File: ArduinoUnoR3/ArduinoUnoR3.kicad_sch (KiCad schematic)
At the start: 40 parts, among them J1 USB_B_Micro, SW1 SW_Push, U1 ATmega16U2-A, U2 LMV358, U3 LMV358, U4 ATmega328PB-A, Y1 16MHz, Y2 16MHz

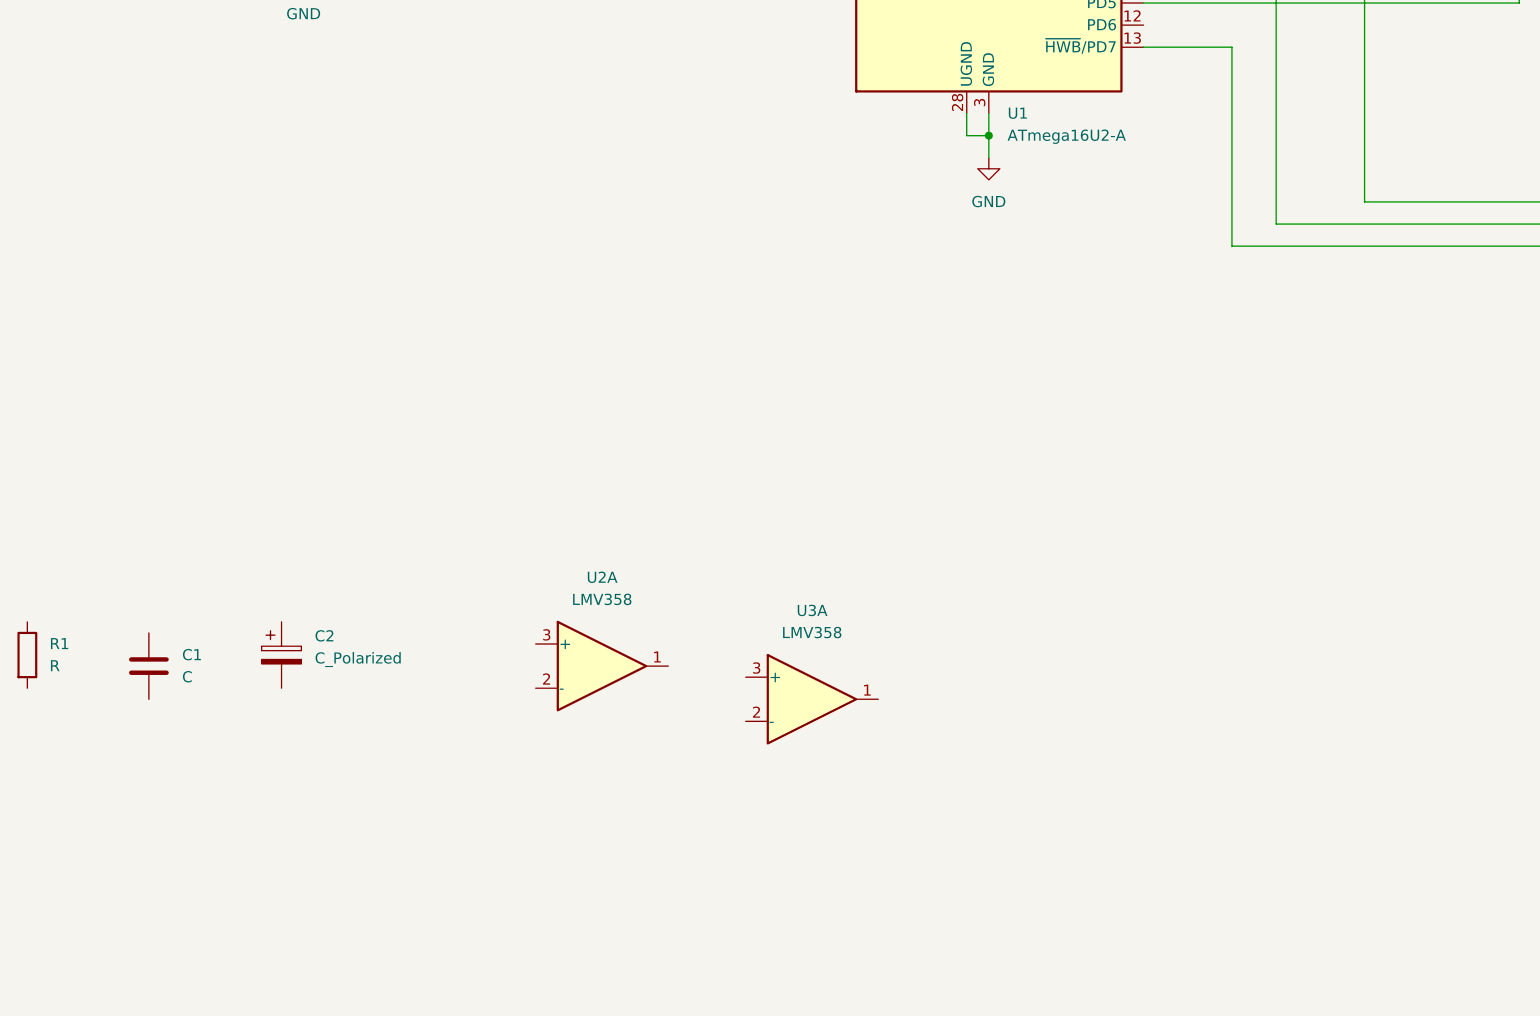
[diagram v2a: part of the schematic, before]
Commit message: added control components to the schematic design
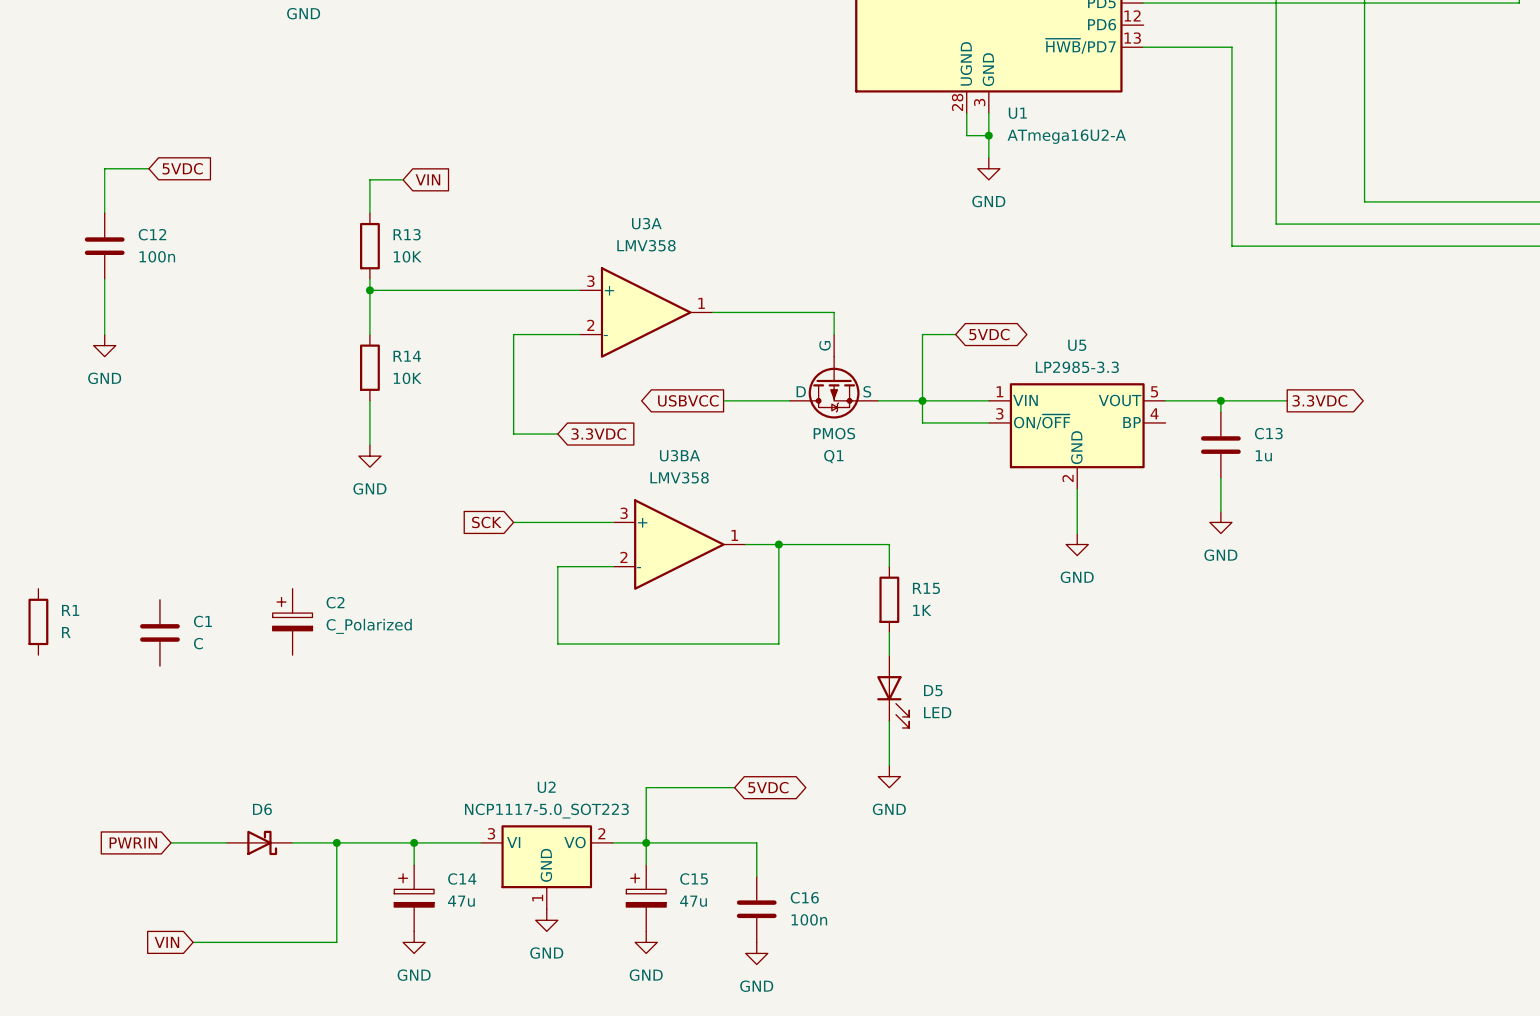
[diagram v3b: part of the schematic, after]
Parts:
- removed U2: LMV358, symbol Amplifier_Operational:LMV358
- added C12, C16: 100n, Capacitor_SMD:C_0603_1608Metric, symbol Device:C
- added C13: 1u, Capacitor_SMD:C_0603_1608Metric, symbol Device:C
- added C14, C15: 47u, Capacitor_SMD:C_0603_1608Metric, symbol Device:C_Polarized
- added D5: LED, symbol Device:LED
- added D6: (no value), Diode_SMD:D_0603_1608Metric, symbol Device:D_Schottky
- added Q1: PMOS, symbol Simulation_SPICE:PMOS
- added R13, R14: 10K, Resistor_SMD:R_0603_1608Metric, symbol Device:R
- added R15: 1K, symbol Device:R
- added U2: NCP1117-5.0_SOT223, Package_TO_SOT_SMD:SOT-223-3_TabPin2, symbol Regulator_Linear:NCP1117-5.0_SOT223
- added U3B: LMV358, symbol Amplifier_Operational:LMV358
- added U5: LP2985-3.3, Package_TO_SOT_SMD:SOT-23-5, symbol Regulator_Linear:LP2985-3.3
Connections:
- net 5VDC: now also C12.1, C15.1, C16.1, Q1.3 (S), U2.2 (VO), U5.1 (VIN), U5.3 (ON/~{OFF})
- net GND: now also C12.2, C13.2, C14.2, C15.2, C16.2, D5.1 (K), R14.2, U2.1 (GND), U5.2 (GND)
- net USBVCC: now also Q1.1 (D)
- net at U3.1: now also Q1.2 (G)
- net 3.3VDC: now reaches U3.2 (-)
- net 3.3VDC: now also C13.1, U5.5 (VOUT)
- net at U3.3 (+): now also R13.2, R14.1
- new net: D5.2 (A), R15.2
- new net: R15.1, U3B.1, U3B.2 (-)
- new net PWRIN: D6.2 (A)
- new net SCK: U3B.3 (+)
- new net VIN: C14.1, D6.1 (K), R13.1, U2.3 (VI)
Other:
- moved on the sheet: C1, C2, R1, U3A

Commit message: Completed the schematic design
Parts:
- removed C1: C, Capacitor_SMD:C_0603_1608Metric, symbol Device:C
- removed C2: C_Polarized, Capacitor_SMD:C_0603_1608Metric, symbol Device:C_Polarized
- removed R1: R, Resistor_SMD:R_0603_1608Metric, symbol Device:R
- removed U3B: LMV358, symbol Amplifier_Operational:LMV358
- added J2, J3: AVR-ISP-6, symbol Connector:AVR-ISP-6
- added J4: Barrel_Jack, symbol Connector:Barrel_Jack
- added unit 2 of U3
- added unit 3 of U3
- D3, D4, D5: footprint (none) -> LED_SMD:LED_0201_0603Metric
- ESD1, ESD2: footprint (none) -> Varistor:RV_Disc_D7mm_W4mm_P5mm
- F1: footprint (none) -> Fuse:Fuse_0603_1608Metric
- L2: footprint (none) -> Inductor_SMD:L_0201_0603Metric
- Q1: footprint (none) -> Package_TO_SOT_SMD:SOT-23
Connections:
- net 5VDC: now also J2.2 (VCC), J3.2 (VCC), U3.8 (V+)
- net GND: now also J2.6 (GND), J3.6 (GND), J4.2, U3.4 (V-)
- net PWRIN: now also J4.1
- net SCK: now also U3.5 (+)
- net USBVCC: now also U1.31 (UVCC)
- net at C11.1, D2.2 (A), R7.2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: now also J3.5 (~{RST})
- net RESET2: now reaches D1.2 (A), R5.2, U1.24 (PC1/~{RESET})
- net RESET2: now also J2.5 (~{RST})
- net at R15.1: now also U3.6 (-), U3.7
- net MOSI: now reaches U4.15 (PB3)
- net MOSI: now also J3.4 (MOSI)
- net MISO: now reaches U4.16 (PB4)
- net MISO: now also J3.1 (MISO)
- net at U4.17 (PB5): now also J3.3 (SCK)
- net SCK2: now reaches U1.15 (PB1)
- net SCK2: now also J2.3 (SCK)
- net MOSI2: now reaches U1.16 (PB2)
- net MOSI2: now also J2.4 (MOSI)
- net MISO2: now reaches U1.17 (PB3)
- net MISO2: now also J2.1 (MISO)
- no-connect marks 0 -> 1
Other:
- moved on the sheet: C10, C11, C12, C13, C14, C15, C16, C3, C4, C5, C6, C7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

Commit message: Added footprints to the components
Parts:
- removed Q1: PMOS, Package_TO_SOT_SMD:SOT-23, symbol Simulation_SPICE:PMOS
- added Q2: FDN340P, Package_TO_SOT_SMD:SOT-23, symbol Transistor_FET:FDN340P
- C14, C15: footprint Capacitor_SMD:C_0603_1608Metric -> Capacitor_SMD:CP_Elec_6.3x5.8
- D3, D4, D5: footprint LED_SMD:LED_0201_0603Metric -> LED_SMD:LED_0603_1608Metric
- J1: footprint (none) -> Connector_USB:USB_Micro-B_Amphenol_10103594-0001LF_Horizontal
- J2, J3: footprint (none) -> Connector_PinHeader_2.54mm:PinHeader_1x01_P2.54mm_Horizontal
- J4: footprint (none) -> Connector_BarrelJack:BarrelJack_SwitchcraftConxall_RAPC10U_Horizontal
- L2: footprint Inductor_SMD:L_0201_0603Metric -> Inductor_SMD:L_0603_1608Metric
- R10, R11, R15: footprint (none) -> Resistor_SMD:R_0603_1608Metric
- SW1: footprint (none) -> Button_Switch_SMD:SW_Tactile_SPST_NO_Straight_CK_PTS636Sx25SMTRLFS
- U3: footprint (none) -> Package_SO:VSSOP-8_3x3mm_P0.65mm
- Y1, Y2: footprint (none) -> Crystal:Crystal_SMD_Abracon_ABM3-2Pin_5.0x3.2mm
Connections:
- net 5VDC: now also Q2.2 (S)
- net USBVCC: now also Q2.3 (D)
- net at U3.1: now also Q2.1 (G)
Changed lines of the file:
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@@
 			)
 		)
-		(property "Footprint" ""
+		(property "Footprint" "Package_SO:VSSOP-8_3x3mm_P0.65mm"
 			(at 41.91 212.09 0)
 			(hide yes)
@@
 			)
 		)
-		(property "Footprint" ""
+		(property "Footprint" "Crystal:Crystal_SMD_Abracon_ABM3-2Pin_5.0x3.2mm"
 			(at 262.89 125.73 0)
 			(hide yes)
@@
 			)
 		)
-		(property "Footprint" ""
+		(property "Footprint" "Resistor_SMD:R_0603_1608Metric"
 			(at 183.642 146.05 90)
 			(hide yes)
@@
 			)
 		)
-		(property "Footprint" ""
+		(property "Footprint" "Connector_PinHeader_2.54mm:PinHeader_1x01_P2.54mm_Horizontal"
 			(at 76.2 69.85 90)
 			(hide yes)
@@
 			)
 		)
-		(property "Footprint" ""
+		(property "Footprint" "Connector_PinHeader_2.54mm:PinHeader_1x01_P2.54mm_Horizontal"
 			(at 209.55 60.96 90)
 			(hide yes)
@@
 			)
 		)
-		(property "Footprint" "LED_SMD:LED_0201_0603Metric"
+		(property "Footprint" "LED_SMD:LED_0603_1608Metric"
 			(at 175.26 156.21 0)
 			(hide yes)
@@
 			)
 		)
-		(property "Footprint" ""
+		(property "Footprint" "Connector_BarrelJack:BarrelJack_SwitchcraftConxall_RAPC10U_Horizontal"
 			(at 21.59 248.666 0)
 			(hide yes)
@@
 			)
 		)
-		(property "Footprint" ""
+		(property "Footprint" "Resistor_SMD:R_0603_1608Metric"
 			(at 173.482 146.05 90)
 			(hide yes)
@@
 			)
 		)
-		(property "Footprint" "Capacitor_SMD:C_0603_1608Metric"
+		(property "Footprint" "Capacitor_SMD:CP_Elec_6.3x5.8"
 			(at 80.9752 269.24 0)
 			(hide yes)
@@
 			)
 		)
-		(property "Footprint" "LED_SMD:LED_0201_0603Metric"
+		(property "Footprint" "LED_SMD:LED_0603_1608Metric"
 			(at 66.04 228.6 0)
 			(hide yes)
@@
 			)
 		)
-		(property "Footprint" ""
+		(property "Footprint" "Resistor_SMD:R_0603_1608Metric"
 			(at 64.262 218.44 90)
 			(hide yes)
@@
 			)
 		)
-		(property "Footprint" ""
+		(property "Footprint" "Connector_USB:USB_Micro-B_Amphenol_10103594-0001LF_Horizontal"
 			(at 30.48 119.38 0)
 			(hide yes)
@@
 	)
 	(symbol
-		(lib_id "Simulation_SPICE:PMOS")
-		(at 185.42 255.27 90)
-		(mirror x)
-		(unit 1)
-		(body_style 1)
-		(exclude_from_sim no)
-		(in_bom yes)
-		(on_board yes)
-		(in_pos_files yes)
-		(dnp no)
-		(property "Reference" "Q1"
-			(at 185.42 264.16 90)
-			(show_name no)
-			(do_not_autoplace no)
-			(effects
-				(font
-					(size 1.27 1.27)
-				)
-			)
-		)
-		(property "Value" "PMOS"
-			(at 185.42 261.62 90)
-			(show_name no)
-			(do_not_autoplace no)
-			(effects
-				(font
-					(size 1.27 1.27)
-				)
-			)
-		)
-		(property "Footprint" "Package_TO_SOT_SMD:SOT-23"
-			(at 182.88 260.35 0)
-			(hide yes)
-			(show_name no)
-			(do_not_autoplace no)
-			(effects
-				(font
-					(size 1.27 1.27)
-				)
-			)
-		)
-		(property "Datasheet" "https://ngspice.sourceforge.io/docs/ngspice-html-manual/manual.xhtml#cha_MOSFETs"
-			(at 198.12 255.27 0)
-			(hide yes)
-			(show_name no)
-			(do_not_autoplace no)
-			(effects
-				(font
-					(size 1.27 1.27)
-				)
-			)
-		)
-		(property "Description" "P-MOSFET transistor, drain/source/gate"
-			(at 185.42 255.27 0)
-			(hide yes)
-			(show_name no)
-			(do_not_autoplace no)
-			(effects
-				(font
-					(size 1.27 1.27)
-				)
-			)
-		)
-		(property "Sim.Device" "PMOS"
-			(at 202.565 255.27 0)
-			(hide yes)
-			(show_name no)
-			(do_not_autoplace no)
-			(effects
-				(font
-					(size 1.27 1.27)
-				)
-			)
-		)
-		(property "Sim.Type" "VDMOS"
-			(at 204.47 255.27 0)
-			(hide yes)
-			(show_name no)
-			(do_not_autoplace no)
-			(effects
-				(font
-					(size 1.27 1.27)
-				)
-			)
-		)
-		(property "Sim.Pins" "1=D 2=G 3=S"
-			(at 200.66 255.27 0)
-			(hide yes)
-			(show_name no)
-			(do_not_autoplace no)
-			(effects
-				(font
-					(size 1.27 1.27)
-				)
-			)
-		)
-		(pin "2"
-		)
-		(pin "3"
-		)
-		(pin "1"
-		)
-		(instances
-			(project "ArduinoUnoR3"
-				(path "/c32b7815-03f3-4c17-970e-8df1fcd87b59"
-					(reference "Q1")
-					(unit 1)
-				)
-			)
-		)
-	)
-	(symbol
 		(lib_id "power:GND")
 		(at 134.62 113.03 0)
@@
 			)
 		)
-		(property "Footprint" "Inductor_SMD:L_0201_0603Metric"
+		(property "Footprint" "Inductor_SMD:L_0603_1608Metric"
 			(at 234.95 102.87 0)
 			(hide yes)
@@
 			)
 		)
-		(property "Footprint" ""
+		(property "Footprint" "Button_Switch_SMD:SW_Tactile_SPST_NO_Straight_CK_PTS636Sx25SMTRLFS"
 			(at 265.43 149.86 0)
 			(hide yes)
@@
 	)
 	(symbol
+		(lib_id "Transistor_FET:FDN340P")
+		(at 185.42 255.27 90)
+		(mirror x)
+		(unit 1)
+		(body_style 1)
+		(exclude_from_sim no)
+		(in_bom yes)
+		(on_board yes)
+		(in_pos_files yes)
+		(dnp no)
+		(property "Reference" "Q2"
+			(at 185.42 261.62 90)
+			(show_name no)
+			(do_not_autoplace no)
+			(effects
+				(font
+					(size 1.27 1.27)
+				)
+			)
+		)
+		(property "Value" "FDN340P"
+			(at 185.42 264.16 90)
+			(show_name no)
+			(do_not_autoplace no)
+			(effects
+				(font
+					(size 1.27 1.27)
+				)
+			)
+		)
+		(property "Footprint" "Package_TO_SOT_SMD:SOT-23"
+			(at 187.325 260.35 0)
+			(hide yes)
+			(show_name no)
+			(do_not_autoplace no)
+			(effects
+				(font
+					(size 1.27 1.27)
+					(italic yes)
+				)
+				(justify left)
+			)
+		)
+		(property "Datasheet" "https://www.onsemi.com/pub/Collateral/FDN340P-D.PDF"
+			(at 189.23 260.35 0)
+			(hide yes)
+			(show_name no)
+			(do_not_autoplace no)
+			(effects
+				(font
+					(size 1.27 1.27)
+				)
+				(justify left)
+			)
+		)
+		(property "Description" "-2A Id, -20V Vds, P-Channel MOSFET, 70mOhm Ron, SOT-23"
+			(at 185.42 255.27 0)
+			(hide yes)
+			(show_name no)
+			(do_not_autoplace no)
+			(effects
+				(font
+					(size 1.27 1.27)
+				)
+			)
+		)
+		(pin "3"
+		)
+		(pin "2"
+		)
+		(pin "1"
+		)
+		(instances
+			(project "ArduinoUnoR3"
+				(path "/c32b7815-03f3-4c17-970e-8df1fcd87b59"
+					(reference "Q2")
+					(unit 1)
+				)
+			)
+		)
+	)
+	(symbol
 		(lib_id "Device:R")
 		(at 100.33 129.54 0)
@@
 			)
 		)
-		(property "Footprint" ""
+		(property "Footprint" "Package_SO:VSSOP-8_3x3mm_P0.65mm"
 			(at 163.83 247.65 0)
 			(hide yes)
@@
 			)
 		)
-		(property "Footprint" ""
+		(property "Footprint" "Crystal:Crystal_SMD_Abracon_ABM3-2Pin_5.0x3.2mm"
 			(at 90.17 128.27 0)
 			(hide yes)
@@
 			)
 		)
-		(property "Footprint" ""
+		(property "Footprint" "Package_SO:VSSOP-8_3x3mm_P0.65mm"
 			(at 102.87 226.06 0)
 			(hide yes)
@@
 			)
 		)
-		(property "Footprint" "Capacitor_SMD:C_0603_1608Metric"
+		(property "Footprint" "Capacitor_SMD:CP_Elec_6.3x5.8"
 			(at 54.3052 269.24 0)
 			(hide yes)
@@
 			)
 		)
-		(property "Footprint" "LED_SMD:LED_0201_0603Metric"
+		(property "Footprint" "LED_SMD:LED_0603_1608Metric"
 			(at 185.42 156.21 0)
 			(hide yes)

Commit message: Added missing footprint for L1
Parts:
- L1: footprint (none) -> Inductor_SMD:L_Taiyo-Yuden_BK_Array_1206_3216Metric
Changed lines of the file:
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@@
 			)
 		)
-		(property "Footprint" ""
+		(property "Footprint" "Inductor_SMD:L_Taiyo-Yuden_BK_Array_1206_3216Metric"
 			(at 43.942 152.4 90)
 			(hide yes)
